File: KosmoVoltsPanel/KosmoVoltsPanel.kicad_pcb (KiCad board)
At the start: 2 copper layers, 10 parts

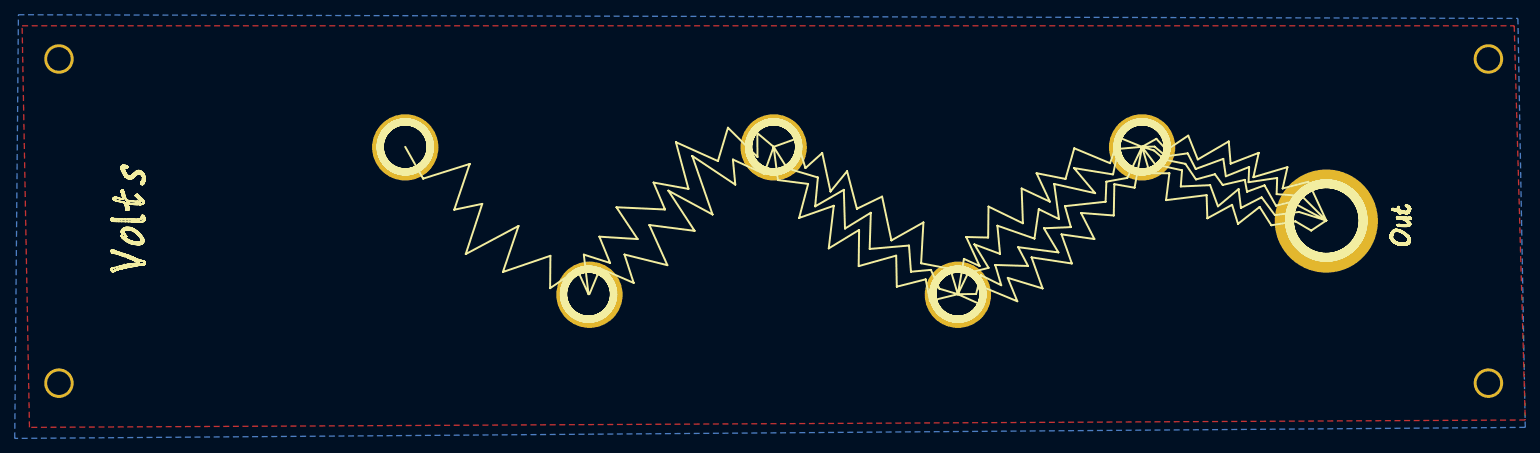
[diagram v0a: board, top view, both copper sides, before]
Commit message: Updated Panel Layout and Graphics
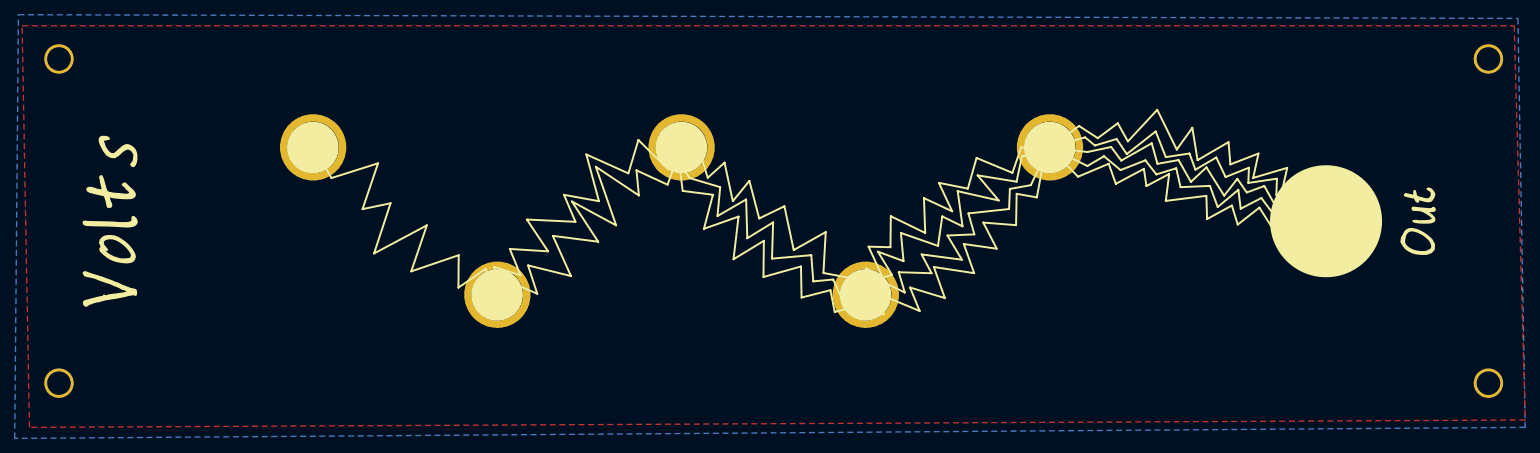
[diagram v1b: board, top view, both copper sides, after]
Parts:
- moved H3 12.5 mm to (167.5, 90.0)
- moved H4 12.5 mm to (67.5, 90.0)
- moved H5 12.5 mm to (92.5, 110.0)
- moved H6 12.5 mm to (117.5, 90.0)
- moved H7 12.5 mm to (142.5, 110.0)

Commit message: Manufacturing Update
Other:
- board outline added: 200 x 50 mm
